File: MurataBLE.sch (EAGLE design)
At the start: 43 parts, among them CON1 C-2235, IC1 I-5448, IC3 74LVC1G00DBV, Q1 FC-135 32.7680KA-AG3, Q2 12MHz, SW1 P8073, SW2 P8073, SW3 P8073, U1 IC_BLE_LBCA2HNZYZ-711, X1 TSW-112-02-S-S

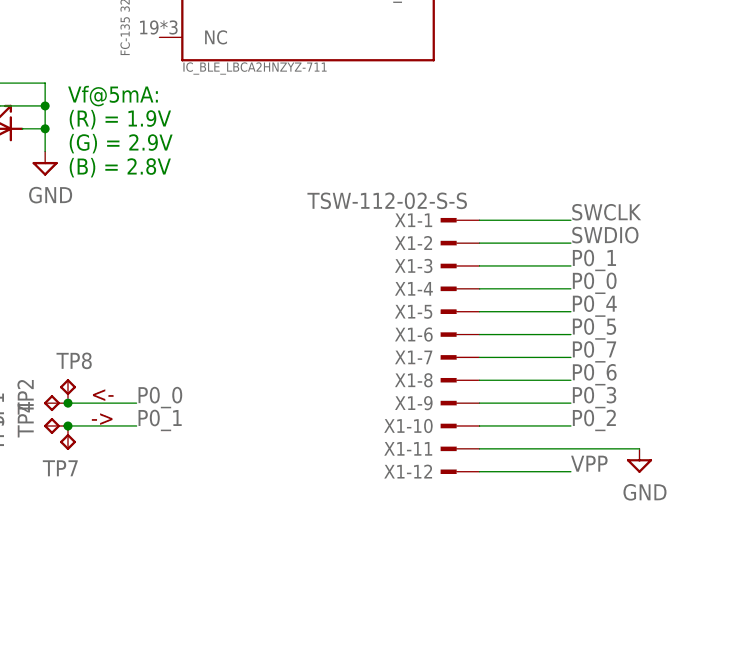
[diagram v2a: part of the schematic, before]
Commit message: [ USB ] extend pin header X1
now ALL pins on header
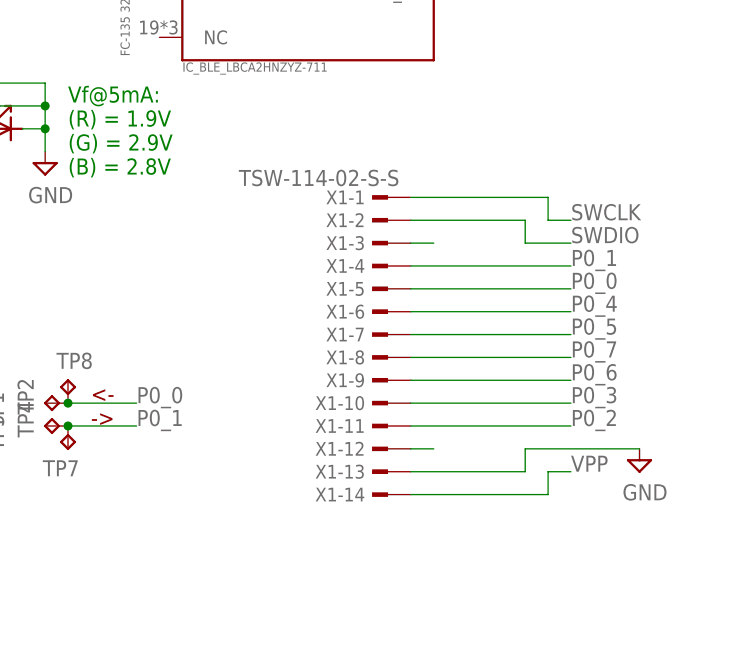
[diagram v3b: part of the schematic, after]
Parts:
- X1: value TSW-112-02-S-S -> TSW-114-02-S-S; device con-samtec.local:TSW-112-02-S-S -> con-samtec.local:TSW-114-02-S-S
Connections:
- net GND: now also X1-13.1; no longer X1-11.1
- net P0_0: now also X1-5.1; no longer X1-4.1
- net P0_1: now also X1-4.1; no longer X1-3.1
- net P0_2: now also X1-11.1; no longer X1-10.1
- net P0_3: now also X1-10.1; no longer X1-9.1
- net P0_4: now also X1-6.1; no longer X1-5.1
- net P0_5: now also X1-7.1; no longer X1-6.1
- net P0_6: now also X1-9.1; no longer X1-8.1
- net P0_7: now also X1-8.1; no longer X1-7.1
- net P1_0: now also X1-3.1
- net P1_1: now also X1-12.1
- net VPP: now also X1-14.1; no longer X1-12.1
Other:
- moved on the sheet: X1-1, X1-10, X1-11, X1-12, X1-2, X1-3, X1-4, X1-5, X1-6, X1-7, X1-8, X1-9
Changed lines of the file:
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@@
 <part name="SUPPLY12" library="mylib" deviceset="GND" device=""/>
 <part name="SUPPLY13" library="mylib" deviceset="GND" device=""/>
-<part name="X1" library="con-samtec.local" deviceset="TSW-112-02-S-S" device=""/>
 <part name="C7" library="mylib" deviceset="C_PAD_PAD_" device="1005" value="18p/1005"/>
 <part name="C10" library="mylib" deviceset="C_PAD_PAD_" device="1005" value="18p/1005"/>
@@
 <part name="TP7" library="testpad_local" deviceset="TP" device="TP06R" value="TPTP06R"/>
 <part name="TP8" library="testpad_local" deviceset="TP" device="TP06R" value="TPTP06R"/>
+<part name="X1" library="con-samtec.local" deviceset="TSW-114-02-S-S" device=""/>
 </parts>
 <sheets>
@@
 <instance part="SUPPLY12" gate="GND" x="86.36" y="66.04"/>
 <instance part="SUPPLY13" gate="GND" x="248.92" y="63.5"/>
-<instance part="X1" gate="-1" x="228.6" y="91.44" rot="MR0"/>
-<instance part="X1" gate="-2" x="228.6" y="88.9" rot="MR0"/>
-<instance part="X1" gate="-3" x="228.6" y="86.36" rot="MR0"/>
-<instance part="X1" gate="-4" x="228.6" y="83.82" rot="MR0"/>
-<instance part="X1" gate="-5" x="228.6" y="81.28" rot="MR0"/>
-<instance part="X1" gate="-6" x="228.6" y="78.74" rot="MR0"/>
-<instance part="X1" gate="-7" x="228.6" y="76.2" rot="MR0"/>
-<instance part="X1" gate="-8" x="228.6" y="73.66" rot="MR0"/>
-<instance part="X1" gate="-9" x="228.6" y="71.12" rot="MR0"/>
-<instance part="X1" gate="-10" x="228.6" y="68.58" rot="MR0"/>
-<instance part="X1" gate="-11" x="228.6" y="66.04" rot="MR0"/>
-<instance part="X1" gate="-12" x="228.6" y="63.5" rot="MR0"/>
 <instance part="C7" gate="G$1" x="66.04" y="83.82" rot="MR0"/>
 <instance part="C10" gate="G$1" x="71.12" y="83.82" rot="MR0"/>
@@
 <instance part="TP7" gate="G$1" x="185.42" y="66.04" rot="R180"/>
 <instance part="TP8" gate="G$1" x="185.42" y="73.66"/>
+<instance part="X1" gate="-1" x="220.98" y="93.98" rot="MR0"/>
+<instance part="X1" gate="-2" x="220.98" y="91.44" rot="MR0"/>
+<instance part="X1" gate="-3" x="220.98" y="88.9" rot="MR0"/>
+<instance part="X1" gate="-4" x="220.98" y="86.36" rot="MR0"/>
+<instance part="X1" gate="-5" x="220.98" y="83.82" rot="MR0"/>
+<instance part="X1" gate="-6" x="220.98" y="81.28" rot="MR0"/>
+<instance part="X1" gate="-7" x="220.98" y="78.74" rot="MR0"/>
+<instance part="X1" gate="-8" x="220.98" y="76.2" rot="MR0"/>
+<instance part="X1" gate="-9" x="220.98" y="73.66" rot="MR0"/>
+<instance part="X1" gate="-10" x="220.98" y="71.12" rot="MR0"/>
+<instance part="X1" gate="-11" x="220.98" y="68.58" rot="MR0"/>
+<instance part="X1" gate="-12" x="220.98" y="66.04" rot="MR0"/>
+<instance part="X1" gate="-13" x="220.98" y="63.5" rot="MR0"/>
+<instance part="X1" gate="-14" x="220.98" y="60.96" rot="MR0"/>
 </instances>
 <busses>
@@
 <segment>
 <pinref part="SUPPLY13" gate="GND" pin="GND"/>
-<wire x1="231.14" y1="66.04" x2="248.92" y2="66.04" width="0.1524" layer="91"/>
-<pinref part="X1" gate="-11" pin="1"/>
+<wire x1="236.22" y1="66.04" x2="248.92" y2="66.04" width="0.1524" layer="91"/>
+<wire x1="223.52" y1="63.5" x2="236.22" y2="63.5" width="0.1524" layer="91"/>
+<wire x1="236.22" y1="63.5" x2="236.22" y2="66.04" width="0.1524" layer="91"/>
+<pinref part="X1" gate="-13" pin="1"/>
 </segment>
 <segment>
@@
 </segment>
 <segment>
-<wire x1="241.3" y1="78.74" x2="231.14" y2="78.74" width="0.1524" layer="91"/>
+<wire x1="241.3" y1="78.74" x2="223.52" y2="78.74" width="0.1524" layer="91"/>
 <label x="241.3" y="78.74" size="1.778" layer="95"/>
-<pinref part="X1" gate="-6" pin="1"/>
+<pinref part="X1" gate="-7" pin="1"/>
 </segment>
 </net>
@@
 </segment>
 <segment>
-<wire x1="241.3" y1="73.66" x2="231.14" y2="73.66" width="0.1524" layer="91"/>
+<wire x1="241.3" y1="73.66" x2="223.52" y2="73.66" width="0.1524" layer="91"/>
 <label x="241.3" y="73.66" size="1.778" layer="95"/>
-<pinref part="X1" gate="-8" pin="1"/>
+<pinref part="X1" gate="-9" pin="1"/>
 </segment>
 </net>
@@
 </segment>
 <segment>
-<wire x1="231.14" y1="76.2" x2="241.3" y2="76.2" width="0.1524" layer="91"/>
+<wire x1="223.52" y1="76.2" x2="241.3" y2="76.2" width="0.1524" layer="91"/>
 <label x="241.3" y="76.2" size="1.778" layer="95"/>
-<pinref part="X1" gate="-7" pin="1"/>
+<pinref part="X1" gate="-8" pin="1"/>
 </segment>
 </net>
@@
 </segment>
 <segment>
-<wire x1="231.14" y1="83.82" x2="241.3" y2="83.82" width="0.1524" layer="91"/>
+<wire x1="223.52" y1="83.82" x2="241.3" y2="83.82" width="0.1524" layer="91"/>
 <label x="241.3" y="83.82" size="1.778" layer="95"/>
-<pinref part="X1" gate="-4" pin="1"/>
+<pinref part="X1" gate="-5" pin="1"/>
 </segment>
 <segment>
@@
 </segment>
 <segment>
-<wire x1="231.14" y1="86.36" x2="241.3" y2="86.36" width="0.1524" layer="91"/>
+<wire x1="223.52" y1="86.36" x2="241.3" y2="86.36" width="0.1524" layer="91"/>
 <label x="241.3" y="86.36" size="1.778" layer="95"/>
-<pinref part="X1" gate="-3" pin="1"/>
+<pinref part="X1" gate="-4" pin="1"/>
 </segment>
 <segment>
@@
 </segment>
 <segment>
-<wire x1="231.14" y1="68.58" x2="241.3" y2="68.58" width="0.1524" layer="91"/>
+<wire x1="223.52" y1="68.58" x2="241.3" y2="68.58" width="0.1524" layer="91"/>
 <label x="241.3" y="68.58" size="1.778" layer="95"/>
-<pinref part="X1" gate="-10" pin="1"/>
+<pinref part="X1" gate="-11" pin="1"/>
 </segment>
 </net>
@@
 </segment>
 <segment>
-<wire x1="231.14" y1="71.12" x2="241.3" y2="71.12" width="0.1524" layer="91"/>
+<wire x1="223.52" y1="71.12" x2="241.3" y2="71.12" width="0.1524" layer="91"/>
 <label x="241.3" y="71.12" size="1.778" layer="95"/>
-<pinref part="X1" gate="-9" pin="1"/>
+<pinref part="X1" gate="-10" pin="1"/>
 </segment>
 </net>
@@
 </segment>
 <segment>
-<wire x1="231.14" y1="81.28" x2="241.3" y2="81.28" width="0.1524" layer="91"/>
+<wire x1="223.52" y1="81.28" x2="241.3" y2="81.28" width="0.1524" layer="91"/>
 <label x="241.3" y="81.28" size="1.778" layer="95"/>
-<pinref part="X1" gate="-5" pin="1"/>
+<pinref part="X1" gate="-6" pin="1"/>
 </segment>
 </net>
@@
 <label x="233.68" y="119.38" size="1.778" layer="95"/>
 </segment>
+<segment>
+<wire x1="223.52" y1="88.9" x2="226.06" y2="88.9" width="0.1524" layer="91"/>
+<pinref part="X1" gate="-3" pin="1"/>
+</segment>
 </net>
 <net name="P1_1" class="0">
@@
 <label x="233.68" y="116.84" size="1.778" layer="95"/>
 </segment>
+<segment>
+<wire x1="226.06" y1="66.04" x2="223.52" y2="66.04" width="0.1524" layer="91"/>
+<pinref part="X1" gate="-12" pin="1"/>
+</segment>
 </net>
 <net name="SWCLK" class="0">
@@
 </segment>
 <segment>
-<wire x1="231.14" y1="91.44" x2="241.3" y2="91.44" width="0.1524" layer="91"/>
+<label x="241.3" y="91.44" size="1.778" layer="95"/>
+<wire x1="238.76" y1="91.44" x2="241.3" y2="91.44" width="0.1524" layer="91"/>
+<wire x1="223.52" y1="93.98" x2="238.76" y2="93.98" width="0.1524" layer="91"/>
+<wire x1="238.76" y1="93.98" x2="238.76" y2="91.44" width="0.1524" layer="91"/>
 <pinref part="X1" gate="-1" pin="1"/>
-<label x="241.3" y="91.44" size="1.778" layer="95"/>
 </segment>
 </net>
@@
 </segment>
 <segment>
-<wire x1="241.3" y1="88.9" x2="231.14" y2="88.9" width="0.1524" layer="91"/>
+<wire x1="241.3" y1="88.9" x2="236.22" y2="88.9" width="0.1524" layer="91"/>
+<label x="241.3" y="88.9" size="1.778" layer="95"/>
+<wire x1="223.52" y1="91.44" x2="236.22" y2="91.44" width="0.1524" layer="91"/>
+<wire x1="236.22" y1="91.44" x2="236.22" y2="88.9" width="0.1524" layer="91"/>
 <pinref part="X1" gate="-2" pin="1"/>
-<label x="241.3" y="88.9" size="1.778" layer="95"/>
 </segment>
 </net>
@@
 </segment>
 <segment>
-<wire x1="241.3" y1="63.5" x2="231.14" y2="63.5" width="0.1524" layer="91"/>
+<wire x1="241.3" y1="63.5" x2="238.76" y2="63.5" width="0.1524" layer="91"/>
 <label x="241.3" y="63.5" size="1.778" layer="95"/>
-<pinref part="X1" gate="-12" pin="1"/>
-</segment>
-</net>
+<wire x1="223.52" y1="60.96" x2="238.76" y2="60.96" width="0.1524" layer="91"/>
+<wire x1="238.76" y1="60.96" x2="238.76" y2="63.5" width="0.1524" layer="91"/>
+<pinref part="X1" gate="-14" pin="1"/>
+</segment>
+</net>

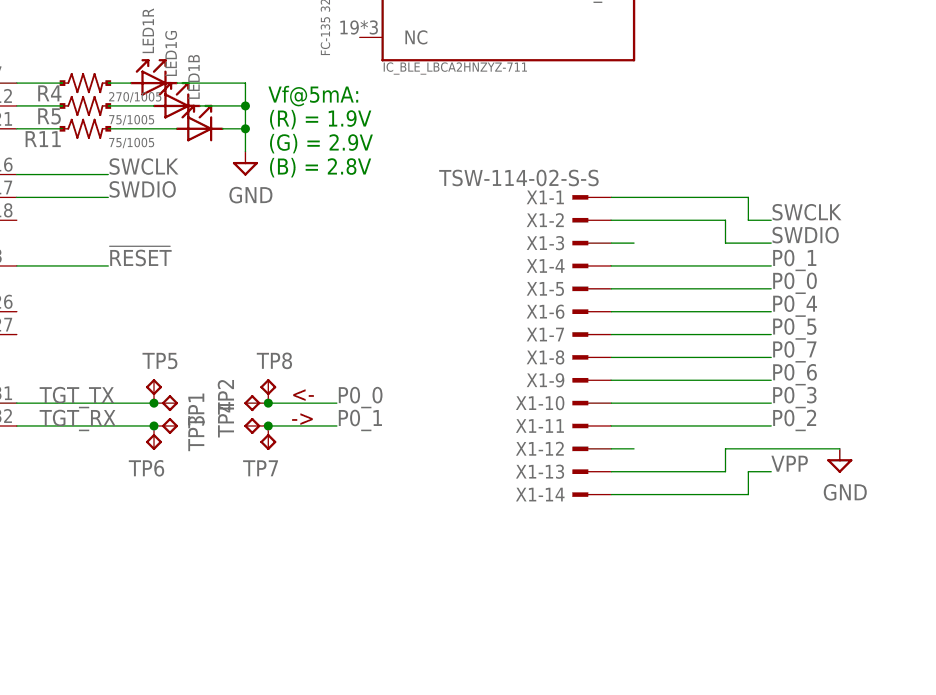
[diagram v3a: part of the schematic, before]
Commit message: [ USB ] update as library
TP
X1 Pin header
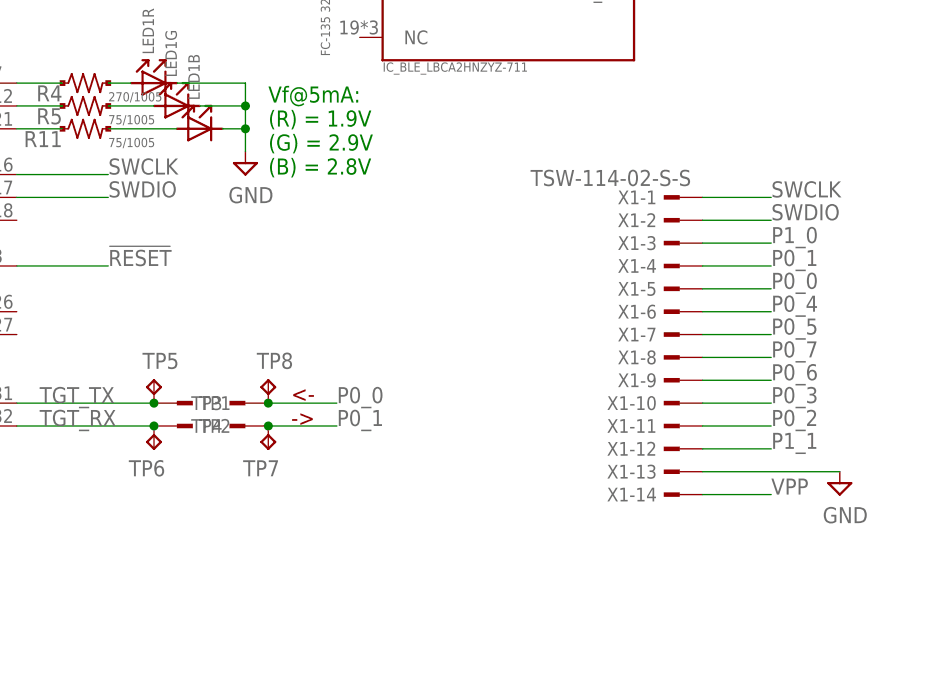
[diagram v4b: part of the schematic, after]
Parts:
- TP1, TP2, TP3, TP4: value TPTP06SQ -> TESTPAD; device testpad_local:TPTP06SQ -> mylib:TESTPAD
- X1: device con-samtec.local:TSW-114-02-S-S -> mylib:TSW-114-02-S-S
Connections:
- net P0_0: now also TP3.1; no longer TP2.TP
- net P0_1: now also TP4.1; no longer TP4.TP
- net TGT_RX: now also TP2.1; no longer TP3.TP
- net TGT_TX: now also TP1.1; no longer TP1.TP
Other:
- moved on the sheet: X1-1, X1-10, X1-11, X1-12, X1-13, X1-14, X1-2, X1-3, X1-4, X1-5, X1-6, X1-7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
